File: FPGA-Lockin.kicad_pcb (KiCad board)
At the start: 4 copper layers, 48.8 x 55.2 mm, 116 parts, among them J1 SPI Header, J2 G125-MH104M4-04AD000P, J3 Laser, J4 PZT, J5 Micro_SD_Card, J6 Conn_02x07_Odd_Even, J7 Conn_01x02_Pin, U1 ICE40UP5K-SG48ITR, U10 OPA310xDBV, U11 MCP1501-30xSN, U12 MCP3561R-E/ST, U13 AD5761RBRUZ-RL7, U14 MIC94090YC6, U15 MCP2562, U2 INA180, U3 SPX3819M5-L-1-2, U4 SPX3819M5-L-2-5, U5 LMR64010XMF, U6 SPX3819M5-L-3-3, U7 STM32F405RGTx, U8 MCP1754S-3302xCB, U9 W25Q32JVSS, Y1 Crystal_GND24

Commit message: Fix Pranav review suggestions
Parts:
- R12: value 16.5mR -> 16mR
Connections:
- C16 pad 2: Net-(D5-A) -> Net-(D5-K)
- D5 pad 1: GNDA -> Net-(D5-K)
- D5 pad 2: Net-(D5-A) -> GNDA
- D5 pad 3: (no net) -> GNDA
- R6 pad 1: Net-(D5-A) -> Net-(D5-K)
- U10 pad 4: Net-(D5-A) -> Net-(D5-K)
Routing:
- net Net-(D5-K): track 0.00 -> 21.5 mm, vias 0 -> 2
- net Net-(D5-A): track 19.2 -> 0.00 mm, vias 1 -> 0
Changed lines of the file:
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@@
 	(net 13 "+3.3VA")
 	(net 14 "Net-(U12-CH0)")
-	(net 15 "Net-(D5-A)")
+	(net 15 "Net-(D5-K)")
 	(net 16 "Net-(U12-AVDD)")
 	(net 17 "Net-(U12-DVDD)")
@@
 			)
 		)
-		(property "Datasheet" "~"
+		(property "Datasheet" "https://www.hamamatsu.com/resources/pdf/ssd/s5971_etc_kpin1025e.pdf"
 			(at 0 0 90)
 			(layer "F.Fab")
@@
 			)
 		)
-		(property "Description" "Photodiode"
+		(property "Description" "Si PIN Photodiode, 0.1 GHz, TO-18-3"
 			(at 0 0 90)
 			(layer "F.Fab")
@@
 			)
 		)
+		(property ki_fp_filters "TO?18*")
 		(sheetname "/Analog/")
 		(sheetfile "analog.kicad_sch")
@@
 			(layers "*.Cu" "*.Mask")
 			(remove_unused_layers no)
-			(net 10 "GNDA")
+			(net 15 "Net-(D5-K)")
 			(pinfunction "K")
 			(pintype "passive")
@@
 			(layers "*.Cu" "*.Mask")
 			(remove_unused_layers no)
-			(net 15 "Net-(D5-A)")
-			(pinfunction "A")
+			(net 10 "GNDA")
+			(pinfunction "C")
 			(pintype "passive")
 		)
@@
 			(layers "*.Cu" "*.Mask")
 			(remove_unused_layers no)
+			(net 10 "GNDA")
+			(pinfunction "A")
+			(pintype "passive")
 		)
 		(embedded_fonts no)
@@
 			(layers "B.Cu" "B.Mask" "B.Paste")
 			(roundrect_rratio 0.25)
-			(net 15 "Net-(D5-A)")
+			(net 15 "Net-(D5-K)")
 			(pinfunction "-")
 			(pintype "input")
@@
 			(layers "B.Cu" "B.Mask" "B.Paste")
 			(roundrect_rratio 0.208333)
-			(net 15 "Net-(D5-A)")
+			(net 15 "Net-(D5-K)")
 			(pintype "passive")
 		)
@@
 			)
 		)
-		(property "Value" "16.5mR"
+		(property "Value" "16mR"
 			(at 0 -1.65 90)
 			(layer "B.Fab")
@@
 			(layers "B.Cu" "B.Mask" "B.Paste")
 			(roundrect_rratio 0.212766)
-			(net 15 "Net-(D5-A)")
+			(net 15 "Net-(D5-K)")
 			(pintype "passive")
 		)
@@
 		(net 15)
 	)
+	(via
+		(at 122.6 67.4)
+		(size 0.762)
+		(drill 0.381)
+		(layers "F.Cu" "B.Cu")
+		(net 15)
+	)
 	(segment
-		(start 123.9375 69.75)
-		(end 124.25 69.75)
+		(start 122.6 67.8)
+		(end 122.6375 67.8375)
 		(width 0.25)
 		(layer "B.Cu")
@@
 	)
 	(segment
-		(start 122.6375 69.8)
-		(end 123.8875 69.8)
+		(start 122.6 67.4)
+		(end 122.6 67.8)
+		(width 0.25)
+		(layer "B.Cu")
+		(net 15)
+	)
+	(segment
+		(start 122.6375 67.8375)
+		(end 122.6375 69.8)
+		(width 0.25)
+		(layer "B.Cu")
+		(net 15)
+	)
+	(segment
+		(start 122.6 67.8)
+		(end 123.55 68.75)
 		(width 0.25)
 		(layer "B.Cu")
@@
 	)
 	(segment
-		(start 124.25 69.75)
+		(start 123.55 68.75)
 		(end 125.25 68.75)
 		(width 0.25)
@@
 	)
 	(segment
-		(start 123.9375 69.75)
-		(end 121 69.75)
+		(start 122.6 67.4)
+		(end 122.6 67.8)
+		(width 0.25)
+		(layer "In1.Cu")
+		(net 15)
+	)
+	(segment
+		(start 117.25 60.650151)
+		(end 117.25 58.5)
+		(width 0.25)
+		(layer "In1.Cu")
+		(net 15)
+	)
+	(segment
+		(start 122.6 67.8)
+		(end 123.9375 69.1375)
+		(width 0.25)
+		(layer "In1.Cu")
+		(net 15)
+	)
+	(segment
+		(start 122.6 66.000151)
+		(end 117.25 60.650151)
 		(width 0.25)
 		(layer "In1.Cu")
@@
 	)
 	(segment
-		(start 121 69.75)
-		(end 114.71 63.46)
+		(start 122.6 67.4)
+		(end 122.6 66.000151)
 		(width 0.25)
 		(layer "In1.Cu")
@@
 	)
 	(segment
-		(start 114.71 63.46)
-		(end 114.71 61.04)
+		(start 123.9375 69.1375)
+		(end 123.9375 69.75)
 		(width 0.25)
 		(layer "In1.Cu")

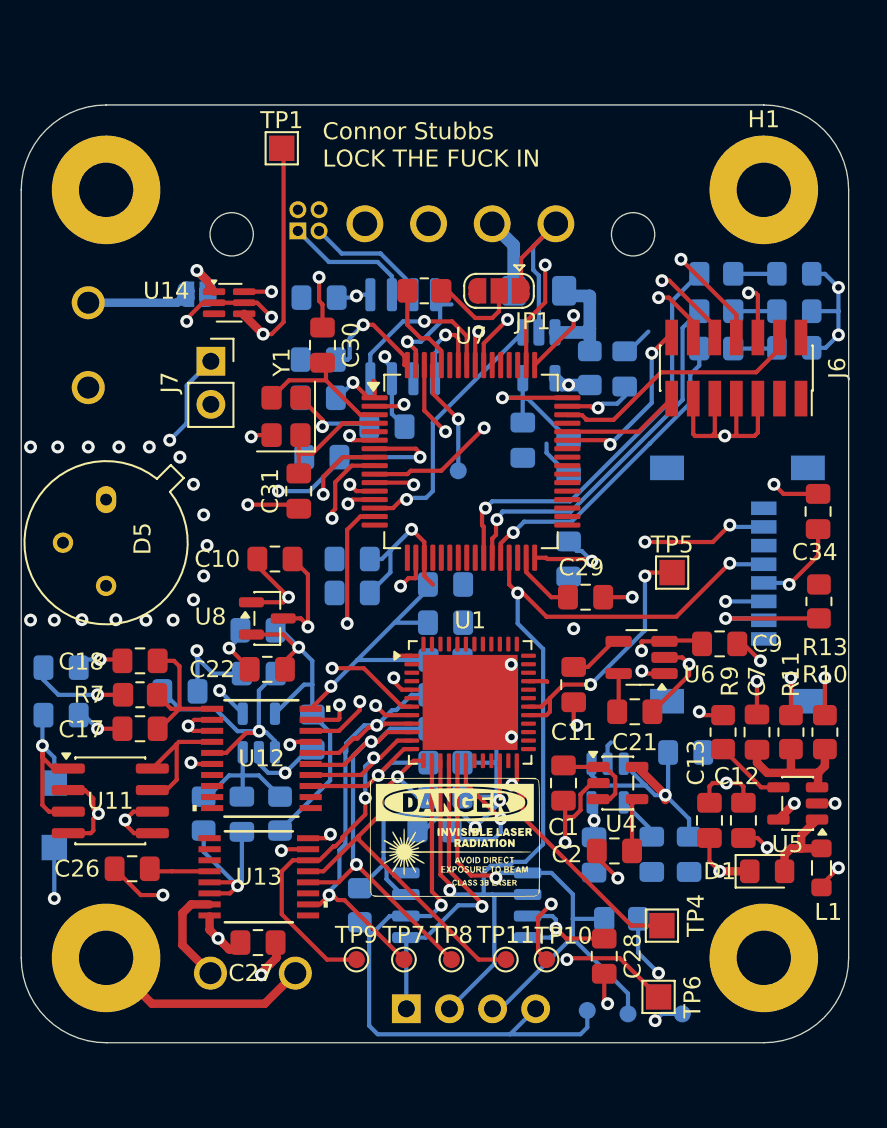
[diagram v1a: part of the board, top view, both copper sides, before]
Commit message: Fix review suggestions from non-fpga board
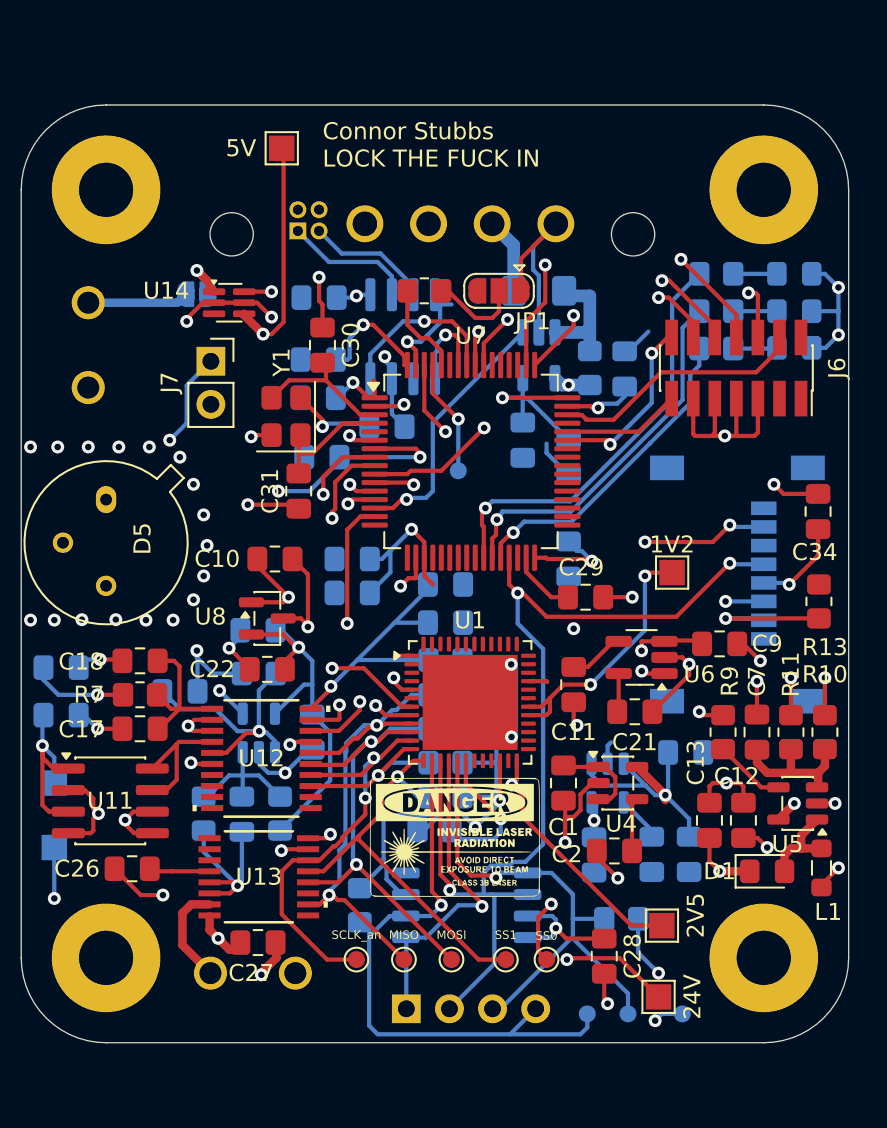
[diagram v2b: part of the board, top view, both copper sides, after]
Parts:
- moved MISO 0.20 mm to (145.6, 88.8)
- renumbered TP5 to 1V2, TP6 to 24V, TP4 to 2V5, TP2 to 3V3, TP3 to 3V3A, TP1 to 5V, TP7 to MISO, TP13 to MISO, TP8 to MOSI, TP12 to MOSI, TP9 to SCLK_an, TP15 to SCLK_m, TP10 to SS0, TP14 to SS0, TP11 to SS1
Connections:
- H2 pad 1: GNDA -> unconnected-(H2-Pad1)
- H3 pad 1: GND -> unconnected-(H3-Pad1)
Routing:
- net GND: track 117.7 -> 104.7 mm
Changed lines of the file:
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@@
 	(net 143 "unconnected-(U7-PA5-Pad21)")
 	(net 144 "unconnected-(U7-PA6-Pad22)")
+	(net 145 "unconnected-(H2-Pad1)")
+	(net 146 "unconnected-(H3-Pad1)")
 	(footprint "Capacitor_SMD:C_0805_2012Metric_Pad1.18x1.45mm_HandSolder"
 		(layer "F.Cu")
@@
 		(descr "SMD pad as test Point, diameter 1.0mm")
 		(tags "test point SMD pad")
-		(property "Reference" "TP11"
+		(property "Reference" "SS1"
 			(at 0 -1.448 0)
 			(layer "F.SilkS")
 			(effects
 				(font
-					(size 1 1)
-					(thickness 0.15)
+					(size 0.5 0.5)
+					(thickness 0.125)
 				)
 			)
@@
 			(layer "F.CrtYd")
 		)
-		(fp_text user "${REFERENCE}"
-			(at 0 -1.45 0)
-			(layer "F.Fab")
-			(effects
-				(font
-					(size 1 1)
-					(thickness 0.15)
-				)
-			)
-		)
 		(pad "1" smd circle
 			(at 0 0)
@@
 		(descr "SMD pad as test Point, diameter 1.0mm")
 		(tags "test point SMD pad")
-		(property "Reference" "TP7"
+		(property "Reference" "MISO"
 			(at 0 -1.448 0)
 			(layer "F.SilkS")
 			(effects
 				(font
-					(size 1 1)
-					(thickness 0.15)
+					(size 0.5 0.5)
+					(thickness 0.125)
 				)
 			)
@@
 			(layer "F.CrtYd")
 		)
-		(fp_text user "${REFERENCE}"
-			(at 0 -1.45 0)
-			(layer "F.Fab")
-			(effects
-				(font
-					(size 1 1)
-					(thickness 0.15)
-				)
-			)
-		)
 		(pad "1" smd circle
 			(at 0 0)
@@
 		(descr "SMD rectangular pad as test Point, square 1.5mm side length")
 		(tags "test point SMD pad rectangle square")
-		(property "Reference" "TP4"
+		(property "Reference" "2V5"
 			(at 2 -0.6 90)
 			(layer "F.SilkS")
@@
 			(at 0 1.75 0)
 			(layer "F.Fab")
+			(hide yes)
 			(effects
 				(font
@@
 			(layer "F.CrtYd")
 		)
-		(fp_text user "${REFERENCE}"
-			(at 0 -1.65 0)
-			(layer "F.Fab")
-			(effects
-				(font
-					(size 1 1)
-					(thickness 0.15)
-				)
-			)
-		)
 		(pad "1" smd rect
 			(at 0 0)
@@
 		(descr "SMD rectangular pad as test Point, square 1.5mm side length")
 		(tags "test point SMD pad rectangle square")
-		(property "Reference" "TP6"
+		(property "Reference" "24V"
 			(at 2 0 90)
 			(layer "F.SilkS")
@@
 			(at 0 1.75 0)
 			(layer "F.Fab")
+			(hide yes)
 			(effects
 				(font
@@
 			(layer "F.CrtYd")
 		)
-		(fp_text user "${REFERENCE}"
-			(at 3 1.4 0)
-			(layer "F.Fab")
-			(effects
-				(font
-					(size 1 1)
-					(thickness 0.15)
-				)
-			)
-		)
 		(pad "1" smd rect
 			(at 0 0)
@@
 		(descr "SMD pad as test Point, diameter 1.0mm")
 		(tags "test point SMD pad")
-		(property "Reference" "TP9"
+		(property "Reference" "SCLK_an"
 			(at 0 -1.448 0)
 			(layer "F.SilkS")
 			(effects
 				(font
-					(size 1 1)
-					(thickness 0.15)
+					(size 0.5 0.5)
+					(thickness 0.125)
 				)
 			)
@@
 			(layer "F.CrtYd")
 		)
-		(fp_text user "${REFERENCE}"
-			(at 0 -1.45 0)
-			(layer "F.Fab")
-			(effects
-				(font
-					(size 1 1)
-					(thickness 0.15)
-				)
-			)
-		)
 		(pad "1" smd circle
 			(at 0 0)
@@
 		(descr "SMD pad as test Point, diameter 1.0mm")
 		(tags "test point SMD pad")
-		(property "Reference" "TP8"
+		(property "Reference" "MOSI"
 			(at 0 -1.448 0)
 			(layer "F.SilkS")
 			(effects
 				(font
-					(size 1 1)
-					(thickness 0.15)
+					(size 0.5 0.5)
+					(thickness 0.125)
 				)
 			)
@@
 			(layer "F.CrtYd")
 		)
-		(fp_text user "${REFERENCE}"
-			(at 0 -1.45 0)
-			(layer "F.Fab")
-			(effects
-				(font
-					(size 1 1)
-					(thickness 0.15)
-				)
-			)
-		)
 		(pad "1" smd circle
 			(at 0 0)
@@
 			(layers "*.Cu" "*.Mask")
 			(remove_unused_layers no)
-			(net 10 "GNDA")
+			(net 145 "unconnected-(H2-Pad1)")
 			(pinfunction "1")
-			(pintype "input")
+			(pintype "input+no_connect")
 			(zone_connect 2)
 		)
@@
 		(descr "SMD rectangular pad as test Point, square 1.5mm side length")
 		(tags "test point SMD pad rectangle square")
-		(property "Reference" "TP5"
+		(property "Reference" "1V2"
 			(at 0 -1.648 0)
 			(layer "F.SilkS")
@@
 			(at 0 1.75 0)
 			(layer "F.Fab")
+			(hide yes)
 			(effects
 				(font
@@
 			(layers "*.Cu" "*.Mask")
 			(remove_unused_layers no)
-			(net 2 "GND")
+			(net 146 "unconnected-(H3-Pad1)")
 			(pinfunction "1")
-			(pintype "input")
+			(pintype "input+no_connect")
 			(zone_connect 2)
 		)
@@
 		(descr "SMD pad as test Point, diameter 1.0mm")
 		(tags "test point SMD pad")
-		(property "Reference" "TP10"
-			(at -1 1.4 0)
+		(property "Reference" "SS0"
+			(at 0 1.4 0)
 			(layer "F.SilkS")
 			(effects
 				(font
-					(size 1 1)
-					(thickness 0.15)
+					(size 0.5 0.5)
+					(thickness 0.125)
 				)
 			)
@@
 			(layer "F.CrtYd")
 		)
-		(fp_text user "${REFERENCE}"
-			(at 0.2 1.998 0)
-			(layer "F.Fab")
-			(effects
-				(font
-					(size 1 1)
-					(thickness 0.15)
-				)
-			)
-		)
 		(pad "1" smd circle
 			(at 0 0 180)
@@
 		(descr "SMD rectangular pad as test Point, square 1.5mm side length")
 		(tags "test point SMD pad rectangle square")
-		(property "Reference" "TP1"
-			(at 0 -1.648 0)
+		(property "Reference" "5V"
+			(at -2.4 0.002 0)
 			(layer "F.SilkS")
 			(effects
@@
 			(at 0 1.75 0)
 			(layer "F.Fab")
+			(hide yes)
 			(effects
 				(font
@@
 		)
 		(fp_text user "${REFERENCE}"
-			(at 0 -1.65 0)
+			(at -2.4 0 0)
 			(layer "F.Fab")
 			(effects
@@
 			(at 0 -4.15 0)
 			(layer "F.SilkS")
+			(hide yes)
 			(effects
 				(font
@@
 		(descr "SMD rectangular pad as test Point, square 1.5mm side length")
 		(tags "test point SMD pad rectangle square")
-		(property "Reference" "TP3"
-			(at -2.4 -0.002 0)
+		(property "Reference" "3V3A"
+			(at -3 0 0)
 			(layer "B.SilkS")
 			(effects
@@
 			(at 0 -1.75 0)
 			(layer "B.Fab")
+			(hide yes)
 			(effects
 				(font
@@
 			(layer "B.CrtYd")
 		)
-		(fp_text user "${REFERENCE}"
-			(at -2.4 0 0)
-			(layer "B.Fab")
-			(effects
-				(font
-					(size 1 1)
-					(thickness 0.15)
-				)
-				(justify mirror)
-			)
-		)
 		(pad "1" smd rect
 			(at 0 0 180)
@@
 	(footprint "TestPoint:TestPoint_Pad_D1.0mm"
 		(layer "B.Cu")
-		(at 145.6 88.6 180)
+		(at 145.6 88.8 180)
 		(descr "SMD pad as test Point, diameter 1.0mm")
 		(tags "test point SMD pad")
-		(property "Reference" "TP13"
+		(property "Reference" "MISO"
 			(at 0 1.448 0)
 			(layer "B.SilkS")
@@
 			(layer "B.CrtYd")
 		)
-		(fp_text user "${REFERENCE}"
-			(at 0 1.45 0)
-			(layer "B.Fab")
-			(effects
-				(font
-					(size 0.5 0.5)
-					(thickness 0.125)
-				)
-				(justify mirror)
-			)
-		)
 		(pad "1" smd circle
 			(at 0 0 180)
@@
 		(descr "SMD pad as test Point, diameter 1.0mm")
 		(tags "test point SMD pad")
-		(property "Reference" "TP12"
+		(property "Reference" "MOSI"
 			(at 0 1.448 0)
 			(layer "B.SilkS")
@@
 			(layer "B.CrtYd")
 		)
-		(fp_text user "${REFERENCE}"
-			(at 0 1.45 0)
-			(layer "B.Fab")
-			(effects
-				(font
-					(size 0.5 0.5)
-					(thickness 0.125)
-				)
-				(justify mirror)
-			)
-		)
 		(pad "1" smd circle
 			(at 0 0 180)
@@
 		(descr "SMD rectangular pad as test Point, square 1.5mm side length")
 		(tags "test point SMD pad rectangle square")
-		(property "Reference" "TP2"
+		(property "Reference" "3V3"
 			(at -2.6 0 0)
 			(layer "B.SilkS")
@@
 			(at 0 -1.75 0)
 			(layer "B.Fab")
+			(hide yes)
 			(effects
 				(font
@@
 			(layer "B.CrtYd")
 		)
-		(fp_text user "${REFERENCE}"
-			(at -2.6 0 0)
-			(layer "B.Fab")
-			(effects
-				(font
-					(size 1 1)
-					(thickness 0.15)
-				)
-				(justify mirror)
-			)
-		)
 		(pad "1" smd rect
 			(at 0 0 180)
@@
 		(descr "SMD pad as test Point, diameter 1.0mm")
 		(tags "test point SMD pad")
-		(property "Reference" "TP14"
+		(property "Reference" "SS0"
 			(at 0 1.448 0)
 			(layer "B.SilkS")
@@
 			)
 		)
-		(fp_text user "PCB edge for Unshielded Cable"
-			(at -8.98 -4 0)
-			(layer "B.Fab")
-			(effects
-				(font
-					(size 0.8 0.8)
-					(thickness 0.15)
-				)
-				(justify mirror)
-			)
-		)
 		(pad "" np_thru_hole circle
 			(at -11.825 3.7)
@@
 		(descr "SMD pad as test Point, diameter 1.0mm")
 		(tags "test point SMD pad")
-		(property "Reference" "TP15"
+		(property "Reference" "SCLK_m"
 			(at 0 1.448 0)
 			(layer "B.SilkS")
@@
 			(layer "B.CrtYd")
 		)
-		(fp_text user "${REFERENCE}"
-			(at 0 1.45 0)
-			(layer "B.Fab")
-			(effects
-				(font
-					(size 0.5 0.5)
-					(thickness 0.125)
-				)
-				(justify mirror)
-			)
-		)
 		(pad "1" smd circle
 			(at 0 0 180)
@@
 	)
 	(segment
-		(start 126.6 88.2)
-		(end 119.95 88.2)
-		(width 0.5)
-		(layer "F.Cu")
-		(net 2)
-	)
-	(segment
 		(start 134.6 63.6)
 		(end 135.068436 63.131564)
@@
 	)
 	(segment
-		(start 128.4 86.4)
-		(end 126.6 88.2)
-		(width 0.5)
-		(layer "F.Cu")
-		(net 2)
-	)
-	(segment
 		(start 140.914867 68.210133)
 		(end 138.7 70.425)
@@
 		(layer "F.Cu")
 		(net 2)
-	)
-	(segment
-		(start 119.95 88.2)
-		(end 117.25 85.5)
-		(width 0.5)
-		(layer "F.Cu")
-		(net 2)
